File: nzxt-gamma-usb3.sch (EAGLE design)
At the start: 7 parts, among them J1 SJ1-3545N, J2 SJ1-3545N, J3 GSB311131HR, J4 GSB311131HR

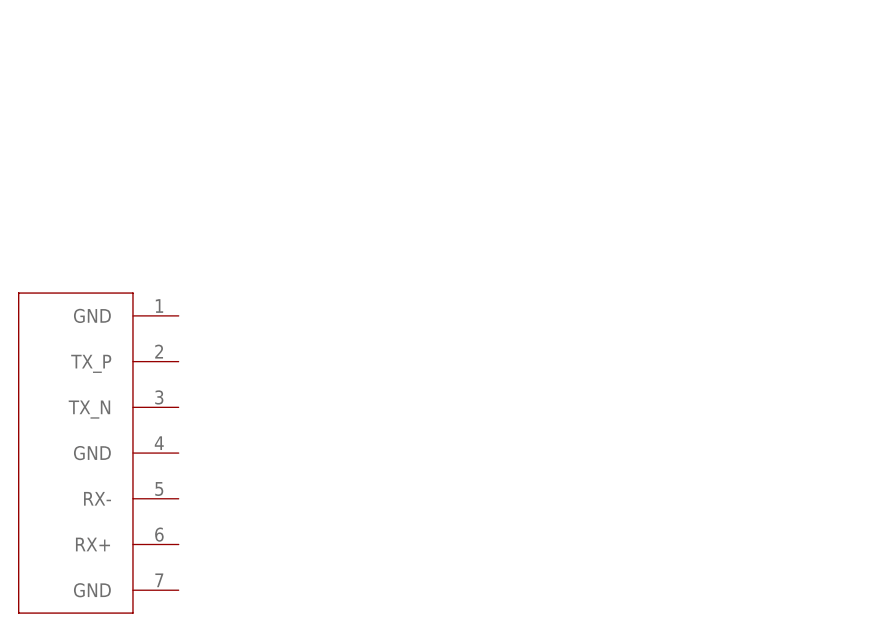
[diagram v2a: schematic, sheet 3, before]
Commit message: Added sata connector. Length matched USB traces. Changed to managed libraries to generate 3D models.
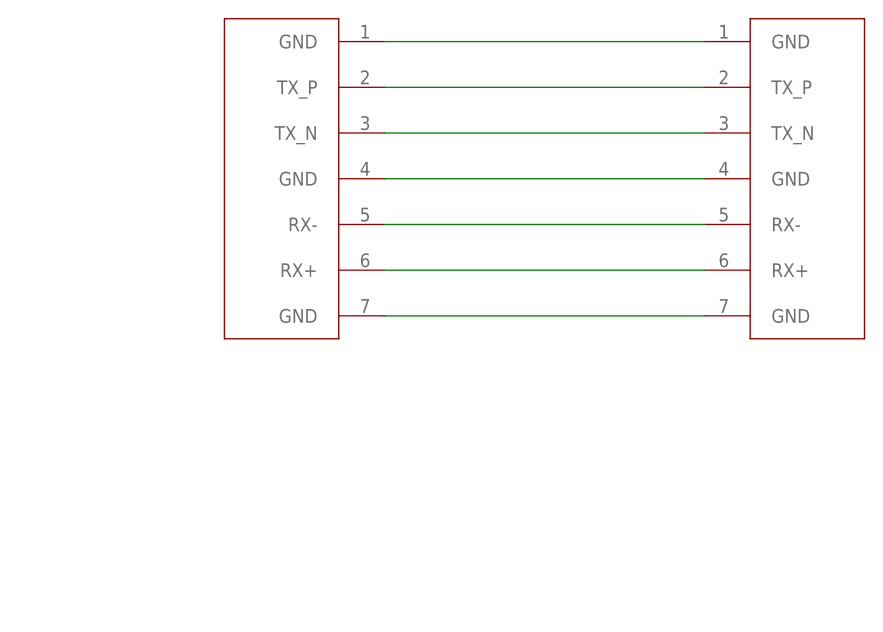
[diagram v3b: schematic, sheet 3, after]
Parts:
- added U$3: 0678007001, dylans-parts:0678007001
- J1, J2: device SJ1-3545N:SJ1-3545N -> dylans-parts:SJ1-3545N
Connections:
- new net N$10: U$2.GND@1, U$3.GND@1
- new net N$11: U$2.GND@2, U$3.GND@2
- new net N$12: U$2.RX+, U$3.RX+
- new net N$13: U$2.RX-, U$3.RX-
- new net N$14: U$2.TX_N, U$3.TX_N
- new net N$15: U$2.TX_P, U$3.TX_P
- new net N$9: U$2.GND@0, U$3.GND@0
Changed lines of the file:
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@@
 <?xml version="1.0" encoding="utf-8"?>
 <!DOCTYPE eagle SYSTEM "eagle.dtd">
-<eagle version="9.1.0">
+<eagle version="9.2.1">
 <drawing>
 <settings>
@@
 <parts>
 <part name="FRAME2" library="frames" library_urn="urn:adsk.eagle:library:229" deviceset="A4L-LOC" device=""/>
-<part name="J1" library="SJ1-3545N" deviceset="SJ1-3545N" device=""/>
-<part name="J2" library="SJ1-3545N" deviceset="SJ1-3545N" device=""/>
+<part name="J1" library="dylans-parts" library_urn="urn:adsk.eagle:library:6331967" deviceset="SJ1-3545N" device="" package3d_urn="urn:adsk.eagle:package:6331970/2"/>
+<part name="J2" library="dylans-parts" library_urn="urn:adsk.eagle:library:6331967" deviceset="SJ1-3545N" device="" package3d_urn="urn:adsk.eagle:package:6331970/2"/>
 <part name="J3" library="GSB311131HR" deviceset="GSB311131HR" device=""/>
 <part name="J4" library="GSB311131HR" deviceset="GSB311131HR" device=""/>
@@
 <part name="U$2" library="G091208300LF" deviceset="G091208300LF" device=""/>
 <part name="FRAME3" library="frames" library_urn="urn:adsk.eagle:library:229" deviceset="A4L-LOC" device=""/>
+<part name="U$3" library="dylans-parts" library_urn="urn:adsk.eagle:library:6331967" deviceset="0678007001" device="" package3d_urn="urn:adsk.eagle:package:6332269/1"/>
 </parts>
 <sheets>
@@
 </plain>
 <instances>
-<instance part="FRAME2" gate="G$1" x="0" y="0"/>
-<instance part="J1" gate="G$1" x="78.74" y="129.54"/>
-<instance part="J2" gate="G$1" x="78.74" y="81.28"/>
-<instance part="JP1" gate="A" x="187.96" y="104.14"/>
-<instance part="AGND1" gate="VR1" x="205.74" y="101.6"/>
-<instance part="AGND2" gate="VR1" x="106.68" y="132.08"/>
-<instance part="AGND3" gate="VR1" x="106.68" y="91.44"/>
+<instance part="FRAME2" gate="G$1" x="0" y="0" smashed="yes">
+<attribute name="DRAWING_NAME" x="217.17" y="15.24" size="2.54" layer="94"/>
+<attribute name="LAST_DATE_TIME" x="217.17" y="10.16" size="2.286" layer="94"/>
+<attribute name="SHEET" x="230.505" y="5.08" size="2.54" layer="94"/>
+</instance>
+<instance part="J1" gate="G$1" x="78.74" y="129.54" smashed="yes">
+<attribute name="NAME" x="71.111659375" y="137.93116875" size="2.54278125" layer="95"/>
+<attribute name="VALUE" x="71.11213125" y="118.6068" size="2.54263125" layer="96"/>
+</instance>
+<instance part="J2" gate="G$1" x="78.74" y="81.28" smashed="yes">
+<attribute name="NAME" x="71.111659375" y="89.67116875" size="2.54278125" layer="95"/>
+<attribute name="VALUE" x="71.11213125" y="70.3468" size="2.54263125" layer="96"/>
+</instance>
+<instance part="JP1" gate="A" x="187.96" y="104.14" smashed="yes">
+<attribute name="NAME" x="181.61" y="112.395" size="1.778" layer="95"/>
+<attribute name="VALUE" x="181.61" y="93.98" size="1.778" layer="96"/>
+</instance>
+<instance part="AGND1" gate="VR1" x="205.74" y="101.6" smashed="yes">
+<attribute name="VALUE" x="203.2" y="96.52" size="1.778" layer="96" rot="R90"/>
+</instance>
+<instance part="AGND2" gate="VR1" x="106.68" y="132.08" smashed="yes">
+<attribute name="VALUE" x="104.14" y="127" size="1.778" layer="96" rot="R90"/>
+</instance>
+<instance part="AGND3" gate="VR1" x="106.68" y="91.44" smashed="yes">
+<attribute name="VALUE" x="104.14" y="86.36" size="1.778" layer="96" rot="R90"/>
+</instance>
 </instances>
 <busses>
@@
 </plain>
 <instances>
-<instance part="J3" gate="G$1" x="53.34" y="111.76" rot="MR0"/>
-<instance part="J4" gate="G$1" x="53.34" y="73.66" rot="MR0"/>
-<instance part="FRAME1" gate="G$1" x="0" y="0"/>
-<instance part="GND1" gate="1" x="68.58" y="55.88"/>
-<instance part="GND2" gate="1" x="68.58" y="93.98"/>
-<instance part="P+1" gate="1" x="68.58" y="129.54"/>
-<instance part="P+2" gate="1" x="68.58" y="91.44"/>
-<instance part="U$1" gate="G$1" x="200.66" y="91.44"/>
-<instance part="P+3" gate="1" x="185.42" y="132.08"/>
-<instance part="GND3" gate="1" x="185.42" y="48.26"/>
+<instance part="J3" gate="G$1" x="53.34" y="111.76" smashed="yes" rot="MR0">
+<attribute name="NAME" x="60.97775" y="127.6719" size="1.782140625" layer="95" rot="MR0"/>
+<attribute name="VALUE" x="60.971959375" y="93.9521" size="1.780790625" layer="96" rot="MR0"/>
+</instance>
+<instance part="J4" gate="G$1" x="53.34" y="73.66" smashed="yes" rot="MR0">
+<attribute name="NAME" x="60.97775" y="89.5719" size="1.782140625" layer="95" rot="MR0"/>
+<attribute name="VALUE" x="60.971959375" y="55.8521" size="1.780790625" layer="96" rot="MR0"/>
+</instance>
+<instance part="FRAME1" gate="G$1" x="0" y="0" smashed="yes">
+<attribute name="DRAWING_NAME" x="217.17" y="15.24" size="2.54" layer="94"/>
+<attribute name="LAST_DATE_TIME" x="217.17" y="10.16" size="2.286" layer="94"/>
+<attribute name="SHEET" x="230.505" y="5.08" size="2.54" layer="94"/>
+</instance>
+<instance part="GND1" gate="1" x="68.58" y="55.88" smashed="yes">
+<attribute name="VALUE" x="66.04" y="53.34" size="1.778" layer="96"/>
+</instance>
+<instance part="GND2" gate="1" x="68.58" y="93.98" smashed="yes">
+<attribute name="VALUE" x="66.04" y="91.44" size="1.778" layer="96"/>
+</instance>
+<instance part="P+1" gate="1" x="68.58" y="129.54" smashed="yes">
+<attribute name="VALUE" x="66.04" y="124.46" size="1.778" layer="96" rot="R90"/>
+</instance>
+<instance part="P+2" gate="1" x="68.58" y="91.44" smashed="yes">
+<attribute name="VALUE" x="66.04" y="86.36" size="1.778" layer="96" rot="R90"/>
+</instance>
+<instance part="U$1" gate="G$1" x="200.66" y="91.44" smashed="yes">
+<attribute name="NAME" x="193.04" y="132.08" size="1.27" layer="95" font="vector"/>
+<attribute name="VALUE" x="193.04" y="48.26" size="1.27" layer="96" font="vector"/>
+</instance>
+<instance part="P+3" gate="1" x="185.42" y="132.08" smashed="yes">
+<attribute name="VALUE" x="182.88" y="127" size="1.778" layer="96" rot="R90"/>
+</instance>
+<instance part="GND3" gate="1" x="185.42" y="48.26" smashed="yes">
+<attribute name="VALUE" x="182.88" y="45.72" size="1.778" layer="96"/>
+</instance>
 </instances>
 <busses>
@@
 </plain>
 <instances>
-<instance part="U$2" gate="G$1" x="53.34" y="68.58" rot="MR0"/>
-<instance part="FRAME3" gate="G$1" x="0" y="0"/>
+<instance part="U$2" gate="G$1" x="76.2" y="99.06" smashed="yes" rot="MR0"/>
+<instance part="FRAME3" gate="G$1" x="0" y="0" smashed="yes">
+<attribute name="DRAWING_NAME" x="217.17" y="15.24" size="2.54" layer="94"/>
+<attribute name="LAST_DATE_TIME" x="217.17" y="10.16" size="2.286" layer="94"/>
+<attribute name="SHEET" x="230.505" y="5.08" size="2.54" layer="94"/>
+</instance>
+<instance part="U$3" gate="G$1" x="121.92" y="99.06" smashed="yes"/>
 </instances>
 <busses>
 </busses>
 <nets>
+<net name="N$9" class="0">
+<segment>
+<pinref part="U$2" gate="G$1" pin="GND@0"/>
+<pinref part="U$3" gate="G$1" pin="GND@0"/>
+<wire x1="81.28" y1="114.3" x2="116.84" y2="114.3" width="0.1524" layer="91"/>
+</segment>
+</net>
+<net name="N$10" class="0">
+<segment>
+<pinref part="U$2" gate="G$1" pin="GND@1"/>
+<pinref part="U$3" gate="G$1" pin="GND@1"/>
+<wire x1="81.28" y1="99.06" x2="116.84" y2="99.06" width="0.1524" layer="91"/>
+</segment>
+</net>
+<net name="N$11" class="0">
+<segment>
+<pinref part="U$3" gate="G$1" pin="GND@2"/>
+<pinref part="U$2" gate="G$1" pin="GND@2"/>
+<wire x1="116.84" y1="83.82" x2="81.28" y2="83.82" width="0.1524" layer="91"/>
+</segment>
+</net>
+<net name="N$12" class="0">
+<segment>
+<pinref part="U$2" gate="G$1" pin="RX+"/>
+<pinref part="U$3" gate="G$1" pin="RX+"/>
+<wire x1="81.28" y1="88.9" x2="116.84" y2="88.9" width="0.1524" layer="91"/>
+</segment>
+</net>
+<net name="N$13" class="0">
+<segment>
+<pinref part="U$3" gate="G$1" pin="RX-"/>
+<pinref part="U$2" gate="G$1" pin="RX-"/>
+<wire x1="116.84" y1="93.98" x2="81.28" y2="93.98" width="0.1524" layer="91"/>
+</segment>
+</net>
+<net name="N$14" class="0">
+<segment>
+<pinref part="U$2" gate="G$1" pin="TX_N"/>
+<pinref part="U$3" gate="G$1" pin="TX_N"/>
+<wire x1="81.28" y1="104.14" x2="116.84" y2="104.14" width="0.1524" layer="91"/>
+</segment>
+</net>
+<net name="N$15" class="0">
+<segment>
+<pinref part="U$3" gate="G$1" pin="TX_P"/>
+<wire x1="116.84" y1="109.22" x2="81.28" y2="109.22" width="0.1524" layer="91"/>
+<pinref part="U$2" gate="G$1" pin="TX_P"/>
+</segment>
+</net>
 </nets>
 </sheet>

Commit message: Updated components on board with better silkscreen
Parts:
- U$1: device usb3_idc:USB_IDC -> dylans-parts:USB_IDC
- U$2: device G091208300LF:G091208300LF -> dylans-parts:G091208300LF
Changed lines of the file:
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@@
 <part name="AGND2" library="supply1" library_urn="urn:adsk.eagle:library:371" deviceset="AGND" device=""/>
 <part name="AGND3" library="supply1" library_urn="urn:adsk.eagle:library:371" deviceset="AGND" device=""/>
-<part name="U$1" library="usb3_idc" deviceset="USB_IDC" device=""/>
+<part name="U$1" library="dylans-parts" library_urn="urn:adsk.eagle:library:6331967" deviceset="USB_IDC" device="" package3d_urn="urn:adsk.eagle:package:6332218/2"/>
 <part name="P+3" library="supply1" library_urn="urn:adsk.eagle:library:371" deviceset="+5V" device=""/>
 <part name="GND3" library="supply1" library_urn="urn:adsk.eagle:library:371" deviceset="GND" device=""/>
-<part name="U$2" library="G091208300LF" deviceset="G091208300LF" device=""/>
+<part name="U$2" library="dylans-parts" library_urn="urn:adsk.eagle:library:6331967" deviceset="G091208300LF" device="" package3d_urn="urn:adsk.eagle:package:6332216/2"/>
 <part name="FRAME3" library="frames" library_urn="urn:adsk.eagle:library:229" deviceset="A4L-LOC" device=""/>
-<part name="U$3" library="dylans-parts" library_urn="urn:adsk.eagle:library:6331967" deviceset="0678007001" device="" package3d_urn="urn:adsk.eagle:package:6332269/1"/>
+<part name="U$3" library="dylans-parts" library_urn="urn:adsk.eagle:library:6331967" deviceset="0678007001" device="" package3d_urn="urn:adsk.eagle:package:6332269/3"/>
 </parts>
 <sheets>

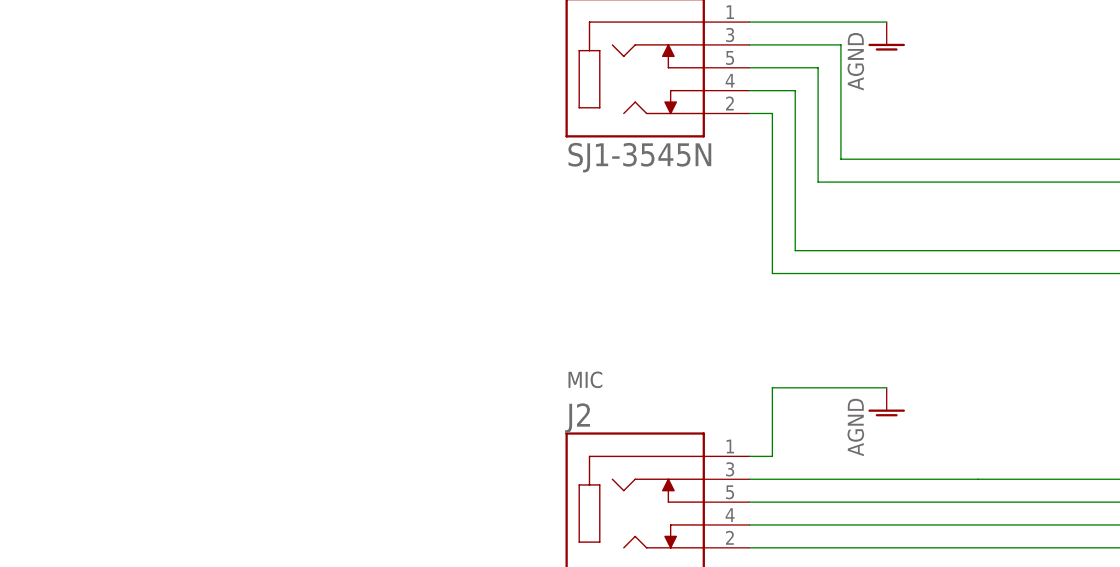
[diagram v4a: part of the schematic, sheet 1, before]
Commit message: Named some nets for debug, added some schematic detail
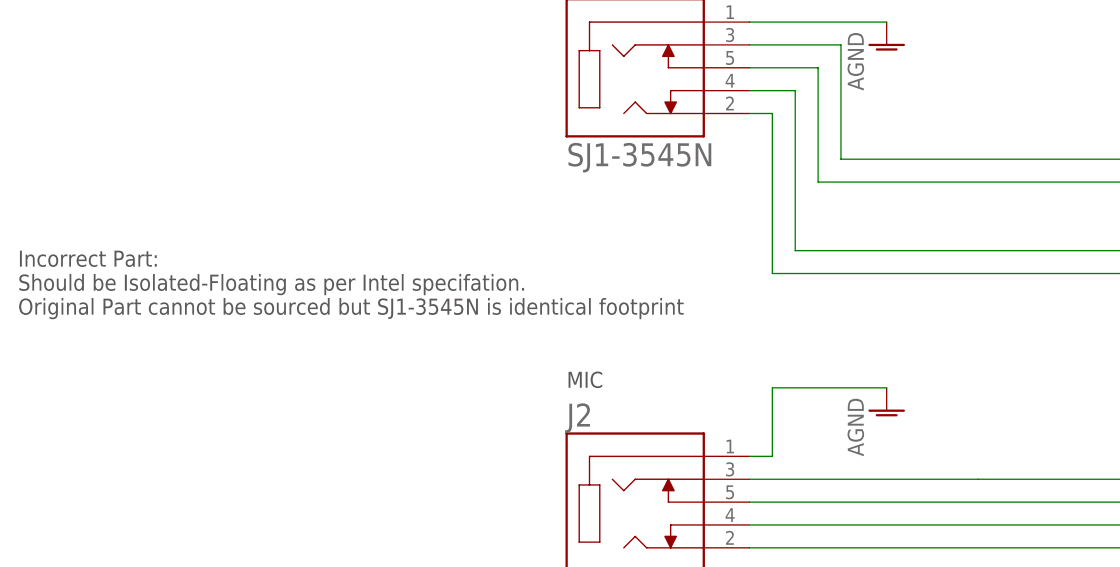
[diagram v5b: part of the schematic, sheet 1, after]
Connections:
- net N$1 renamed SENSE_1_RET
- net N$3 renamed SENSE1_1_SEND
- net N$4 renamed P_1_R
- net N$5 renamed P_2_L
- net N$6 renamed SENSE_2_RET
- net N$8 renamed P_2_R
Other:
- note added: "Incorrect Part: Should be Isolated-Floating as per Intel specifation. Original Part cannot be sourced but SJ1-3545N is identical footprint"
- note added: "eSATA"
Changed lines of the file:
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@@
 <parts>
 <part name="FRAME2" library="frames" library_urn="urn:adsk.eagle:library:229" deviceset="A4L-LOC" device=""/>
-<part name="J1" library="dylans-parts" library_urn="urn:adsk.eagle:library:6331967" deviceset="SJ1-3545N" device="" package3d_urn="urn:adsk.eagle:package:6331970/2"/>
-<part name="J2" library="dylans-parts" library_urn="urn:adsk.eagle:library:6331967" deviceset="SJ1-3545N" device="" package3d_urn="urn:adsk.eagle:package:6331970/2"/>
+<part name="J1" library="dylans-parts" library_urn="urn:adsk.eagle:library:6331967" deviceset="SJ1-3545N" device="" package3d_urn="urn:adsk.eagle:package:6331970/3"/>
+<part name="J2" library="dylans-parts" library_urn="urn:adsk.eagle:library:6331967" deviceset="SJ1-3545N" device="" package3d_urn="urn:adsk.eagle:package:6331970/3"/>
 <part name="J3" library="GSB311131HR" deviceset="GSB311131HR" device=""/>
 <part name="J4" library="GSB311131HR" deviceset="GSB311131HR" device=""/>
@@
 <text x="71.12" y="142.24" size="1.778" layer="97" font="vector">Headphone</text>
 <text x="71.12" y="93.98" size="1.778" layer="97" font="vector">MIC</text>
+<text x="10.16" y="109.22" size="1.778" layer="97" font="vector" align="top-left">Incorrect Part:
+Should be Isolated-Floating as per Intel specifation.
+Original Part cannot be sourced but SJ1-3545N is identical footprint</text>
 </plain>
 <instances>
@@
 </segment>
 </net>
-<net name="N$1" class="0">
+<net name="SENSE_1_RET" class="0">
 <segment>
 <pinref part="JP1" gate="A" pin="10"/>
@@
 </segment>
 </net>
-<net name="N$5" class="0">
+<net name="P_2_L" class="0">
 <segment>
 <pinref part="J1" gate="G$1" pin="2"/>
@@
 </segment>
 </net>
-<net name="N$6" class="0">
+<net name="SENSE_2_RET" class="0">
 <segment>
 <pinref part="JP1" gate="A" pin="1"/>
@@
 </segment>
 </net>
-<net name="N$4" class="0">
+<net name="P_1_R" class="0">
 <segment>
 <pinref part="JP1" gate="A" pin="7"/>
@@
 </segment>
 </net>
-<net name="N$3" class="0">
+<net name="SENSE1_1_SEND" class="0">
 <segment>
 <pinref part="JP1" gate="A" pin="2"/>
@@
 </segment>
 </net>
-<net name="N$8" class="0">
+<net name="P_2_R" class="0">
 <segment>
 <pinref part="JP1" gate="A" pin="4"/>
@@
 <sheet>
 <plain>
+<text x="218.44" y="20.32" size="1.778" layer="94" font="vector">eSATA</text>
 </plain>
 <instances>
@@
 </drawing>
 <compatibility>
+<note version="6.3" minversion="6.2.2" severity="warning">
+Since Version 6.2.2 text objects can contain more than one line,
+which will not be processed correctly with this version.
+</note>
 <note version="8.2" severity="warning">
 Since Version 8.2, EAGLE supports online libraries. The ids
